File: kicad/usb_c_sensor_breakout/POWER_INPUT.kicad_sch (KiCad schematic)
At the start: 5 parts, among them J1 USB_C_Receptacle_PowerOnly_6P

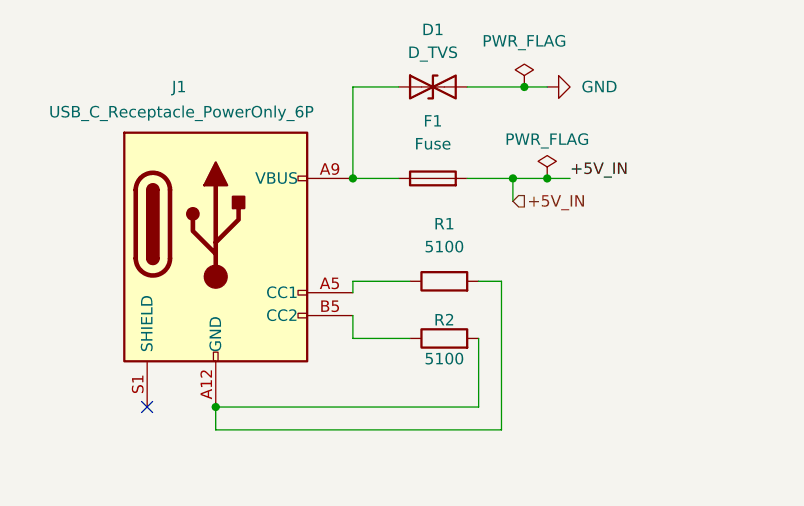
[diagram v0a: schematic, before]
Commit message: Commit3: Regulators + Top-level + I2C sensor upgrade
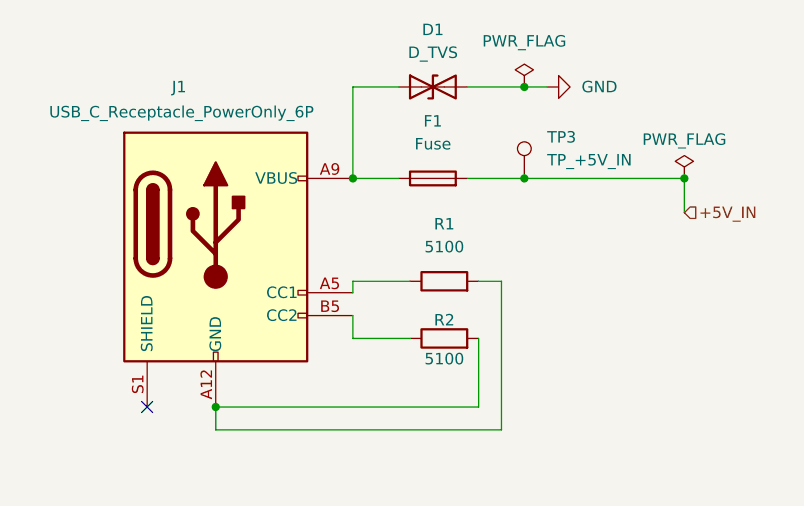
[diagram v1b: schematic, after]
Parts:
- added TP3: TP_+5V_IN, symbol Connector:TestPoint
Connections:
- net +5V_IN: now also TP3.1
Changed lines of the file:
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@@
 	(paper "A4")
-	(junction
-		(at 119.38 83.82)
-		(diameter 0)
-		(color 0 0 0 0)
-	)
 	(junction
 		(at 82.55 109.22)
@@
 	)
 	(junction
-		(at 115.57 83.82)
+		(at 116.84 83.82)
+		(diameter 0)
+		(color 0 0 0 0)
+	)
+	(junction
+		(at 134.62 83.82)
 		(diameter 0)
 		(color 0 0 0 0)
@@
 	(wire
 		(pts
-			(xy 115.57 83.82) (xy 119.38 83.82)
-		)
-		(stroke
-			(width 0)
-			(type default)
-		)
-	)
-	(wire
-		(pts
 			(xy 116.84 73.66) (xy 119.38 73.66)
 		)
@@
 	(wire
 		(pts
+			(xy 116.84 83.82) (xy 134.62 83.82)
+		)
+		(stroke
+			(width 0)
+			(type default)
+		)
+	)
+	(wire
+		(pts
 			(xy 97.79 83.82) (xy 97.79 73.66)
 		)
@@
 	(wire
 		(pts
-			(xy 119.38 83.82) (xy 121.92 83.82)
-		)
-		(stroke
-			(width 0)
-			(type default)
-		)
-	)
-	(wire
-		(pts
 			(xy 97.79 73.66) (xy 102.87 73.66)
 		)
@@
 	(wire
 		(pts
-			(xy 115.57 86.36) (xy 115.57 83.82)
+			(xy 134.62 83.82) (xy 134.62 87.63)
 		)
 		(stroke
@@
 	(wire
 		(pts
-			(xy 110.49 83.82) (xy 115.57 83.82)
-		)
-		(stroke
-			(width 0)
-			(type default)
-		)
-	)
-	(label "+5V_IN"
-		(at 121.92 83.82 0)
-		(effects
-			(font
-				(size 1.27 1.27)
-			)
-			(justify left bottom)
+			(xy 110.49 83.82) (xy 116.84 83.82)
+		)
+		(stroke
+			(width 0)
+			(type default)
 		)
 	)
 	(hierarchical_label "+5V_IN"
 		(shape input)
-		(at 115.57 86.36 0)
+		(at 134.62 87.63 0)
 		(effects
 			(font
@@
 	(symbol
 		(lib_id "power:PWR_FLAG")
-		(at 119.38 83.82 0)
+		(at 134.62 83.82 0)
 		(unit 1)
 		(exclude_from_sim no)
@@
 		(dnp no)
 		(property "Reference" "#FLG0101"
-			(at 119.38 81.915 0)
+			(at 134.62 81.915 0)
 			(effects
 				(font
@@
 		)
 		(property "Value" "PWR_FLAG"
-			(at 119.38 79.502 0)
+			(at 134.62 79.502 0)
 			(effects
 				(font
@@
 		)
 		(property "Footprint" ""
-			(at 119.38 83.82 0)
+			(at 134.62 83.82 0)
 			(effects
 				(font
@@
 		)
 		(property "Datasheet" "~"
-			(at 119.38 83.82 0)
+			(at 134.62 83.82 0)
 			(effects
 				(font
@@
 		)
 		(property "Description" "Special symbol for telling ERC where power comes from"
-			(at 119.38 83.82 0)
+			(at 134.62 83.82 0)
 			(effects
 				(font
@@
 					(unit 1)
 				)
+			)
+		)
+	)
+	(symbol
+		(lib_id "Connector:TestPoint")
+		(at 116.84 83.82 0)
+		(unit 1)
+		(exclude_from_sim no)
+		(in_bom yes)
+		(on_board yes)
+		(dnp no)
+		(fields_autoplaced yes)
+		(property "Reference" "TP3"
+			(at 119.38 79.2479 0)
+			(effects
+				(font
+					(size 1.27 1.27)
+				)
+				(justify left)
+			)
+		)
+		(property "Value" "TP_+5V_IN"
+			(at 119.38 81.7879 0)
+			(effects
+				(font
+					(size 1.27 1.27)
+				)
+				(justify left)
+			)
+		)
+		(property "Footprint" ""
+			(at 121.92 83.82 0)
+			(effects
+				(font
+					(size 1.27 1.27)
+				)
+				(hide yes)
+			)
+		)
+		(property "Datasheet" "~"
+			(at 121.92 83.82 0)
+			(effects
+				(font
+					(size 1.27 1.27)
+				)
+				(hide yes)
+			)
+		)
+		(property "Description" "test point"
+			(at 116.84 83.82 0)
+			(effects
+				(font
+					(size 1.27 1.27)
+				)
+				(hide yes)
+			)
+		)
+		(pin "1"
+		)
+		(instances
+			(project ""
+				(path "/a2072585-dfc7-469c-b616-14a83342abb9/2cb23028-9002-4014-b3cb-b730b7692fef"
+					(reference "TP3")
+					(unit 1)
+				)

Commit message: Commit 4: Updated annotation + footprints
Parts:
- D1: footprint (none) -> Diode_SMD:D_SOD-123
- F1: footprint (none) -> Fuse:Fuse_1812_4532Metric
- J1: footprint (none) -> Connector_USB:USB_C_Receptacle_HRO_TYPE-C-31-M-12
- R1, R2: footprint (none) -> Resistor_SMD:R_0603_1608Metric
- TP3: footprint (none) -> TestPoint:TestPoint_Pad_D1.5mm
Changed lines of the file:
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@@
 			)
 		)
-		(property "Footprint" ""
+		(property "Footprint" "Resistor_SMD:R_0603_1608Metric"
 			(at 107.95 97.028 90)
 			(effects
@@
 			)
 		)
-		(property "Footprint" ""
+		(property "Footprint" "Fuse:Fuse_1812_4532Metric"
 			(at 106.68 85.598 90)
 			(effects
@@
 			)
 		)
-		(property "Footprint" ""
+		(property "Footprint" "Resistor_SMD:R_0603_1608Metric"
 			(at 107.95 103.378 90)
 			(effects
@@
 			)
 		)
-		(property "Footprint" ""
+		(property "Footprint" "Connector_USB:USB_C_Receptacle_HRO_TYPE-C-31-M-12"
 			(at 86.36 88.9 0)
 			(effects
@@
 			)
 		)
-		(property "Footprint" ""
+		(property "Footprint" "Diode_SMD:D_SOD-123"
 			(at 106.68 73.66 0)
 			(effects
@@
 			)
 		)
-		(property "Footprint" ""
+		(property "Footprint" "TestPoint:TestPoint_Pad_D1.5mm"
 			(at 121.92 83.82 0)
 			(effects

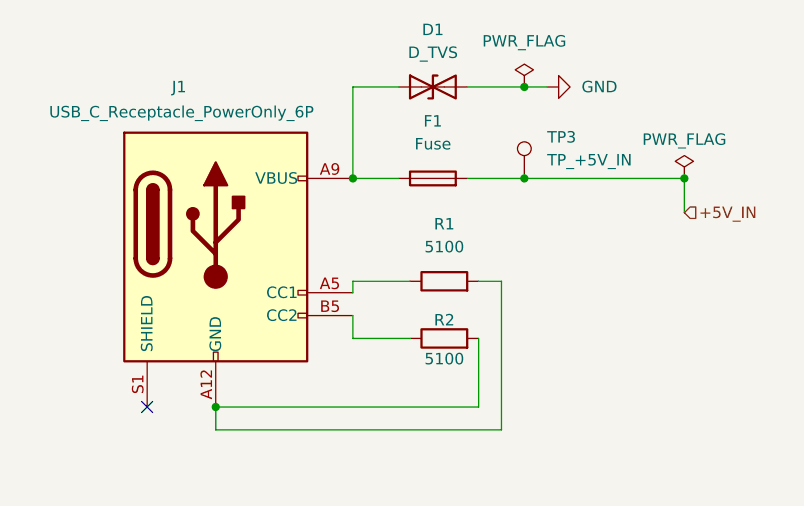
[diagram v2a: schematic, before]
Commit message: Commit 5: MCU + Final Schematic Touches + Labelling + USBc fix
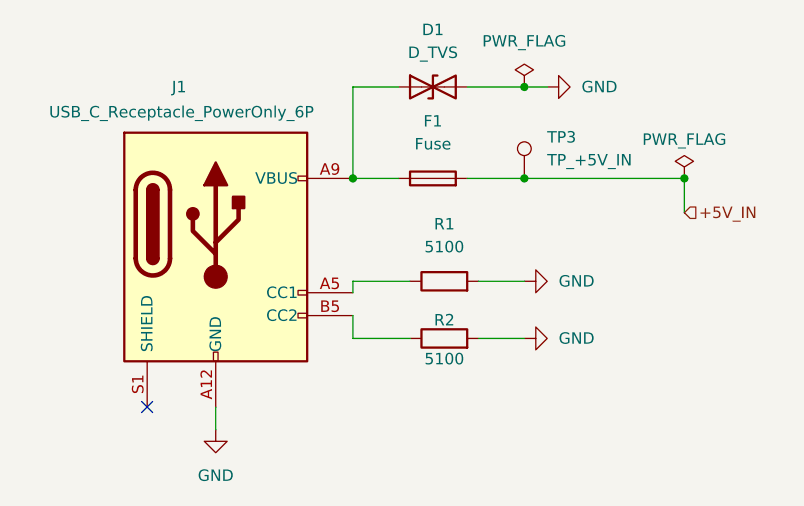
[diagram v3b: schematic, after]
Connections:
- net GND: now also J1.A12 (GND), J1.B12 (GND), R1.2, R2.2
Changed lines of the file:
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@@
 	(paper "A4")
-	(junction
-		(at 82.55 109.22)
-		(diameter 0)
-		(color 0 0 0 0)
-	)
 	(junction
 		(at 116.84 73.66)
@@
 	(wire
 		(pts
-			(xy 114.3 95.25) (xy 114.3 111.76)
-		)
-		(stroke
-			(width 0)
-			(type default)
-		)
-	)
-	(wire
-		(pts
 			(xy 116.84 83.82) (xy 134.62 83.82)
 		)
@@
 	(wire
 		(pts
+			(xy 111.76 101.6) (xy 116.84 101.6)
+		)
+		(stroke
+			(width 0)
+			(type default)
+		)
+	)
+	(wire
+		(pts
 			(xy 97.79 73.66) (xy 102.87 73.66)
 		)
@@
 	(wire
 		(pts
-			(xy 82.55 109.22) (xy 111.76 109.22)
-		)
-		(stroke
-			(width 0)
-			(type default)
-		)
-	)
-	(wire
-		(pts
 			(xy 97.79 95.25) (xy 104.14 95.25)
 		)
@@
 	(wire
 		(pts
-			(xy 114.3 111.76) (xy 82.55 111.76)
-		)
-		(stroke
-			(width 0)
-			(type default)
-		)
-	)
-	(wire
-		(pts
 			(xy 134.62 83.82) (xy 134.62 87.63)
 		)
@@
 	(wire
 		(pts
-			(xy 111.76 109.22) (xy 111.76 101.6)
-		)
-		(stroke
-			(width 0)
-			(type default)
-		)
-	)
-	(wire
-		(pts
-			(xy 111.76 95.25) (xy 114.3 95.25)
-		)
-		(stroke
-			(width 0)
-			(type default)
-		)
-	)
-	(wire
-		(pts
 			(xy 110.49 83.82) (xy 116.84 83.82)
+		)
+		(stroke
+			(width 0)
+			(type default)
+		)
+	)
+	(wire
+		(pts
+			(xy 111.76 95.25) (xy 116.84 95.25)
 		)
 		(stroke
@@
 	)
 	(symbol
+		(lib_id "power:GND")
+		(at 116.84 101.6 90)
+		(unit 1)
+		(exclude_from_sim no)
+		(in_bom yes)
+		(on_board yes)
+		(dnp no)
+		(fields_autoplaced yes)
+		(property "Reference" "#PWR014"
+			(at 123.19 101.6 0)
+			(effects
+				(font
+					(size 1.27 1.27)
+				)
+				(hide yes)
+			)
+		)
+		(property "Value" "GND"
+			(at 120.65 101.5999 90)
+			(effects
+				(font
+					(size 1.27 1.27)
+				)
+				(justify right)
+			)
+		)
+		(property "Footprint" ""
+			(at 116.84 101.6 0)
+			(effects
+				(font
+					(size 1.27 1.27)
+				)
+				(hide yes)
+			)
+		)
+		(property "Datasheet" ""
+			(at 116.84 101.6 0)
+			(effects
+				(font
+					(size 1.27 1.27)
+				)
+				(hide yes)
+			)
+		)
+		(property "Description" "Power symbol creates a global label with name \"GND\" , ground"
+			(at 116.84 101.6 0)
+			(effects
+				(font
+					(size 1.27 1.27)
+				)
+				(hide yes)
+			)
+		)
+		(pin "1"
+		)
+		(instances
+			(project ""
+				(path "/a2072585-dfc7-469c-b616-14a83342abb9/2cb23028-9002-4014-b3cb-b730b7692fef"
+					(reference "#PWR014")
+					(unit 1)
+				)
+			)
+		)
+	)
+	(symbol
 		(lib_id "power:PWR_FLAG")
 		(at 134.62 83.82 0)
@@
 	)
 	(symbol
+		(lib_id "power:GND")
+		(at 82.55 111.76 0)
+		(unit 1)
+		(exclude_from_sim no)
+		(in_bom yes)
+		(on_board yes)
+		(dnp no)
+		(fields_autoplaced yes)
+		(property "Reference" "#PWR013"
+			(at 82.55 118.11 0)
+			(effects
+				(font
+					(size 1.27 1.27)
+				)
+				(hide yes)
+			)
+		)
+		(property "Value" "GND"
+			(at 82.55 116.84 0)
+			(effects
+				(font
+					(size 1.27 1.27)
+				)
+			)
+		)
+		(property "Footprint" ""
+			(at 82.55 111.76 0)
+			(effects
+				(font
+					(size 1.27 1.27)
+				)
+				(hide yes)
+			)
+		)
+		(property "Datasheet" ""
+			(at 82.55 111.76 0)
+			(effects
+				(font
+					(size 1.27 1.27)
+				)
+				(hide yes)
+			)
+		)
+		(property "Description" "Power symbol creates a global label with name \"GND\" , ground"
+			(at 82.55 111.76 0)
+			(effects
+				(font
+					(size 1.27 1.27)
+				)
+				(hide yes)
+			)
+		)
+		(pin "1"
+		)
+		(instances
+			(project ""
+				(path "/a2072585-dfc7-469c-b616-14a83342abb9/2cb23028-9002-4014-b3cb-b730b7692fef"
+					(reference "#PWR013")
+					(unit 1)
+				)
+			)
+		)
+	)
+	(symbol
 		(lib_id "Connector:USB_C_Receptacle_PowerOnly_6P")
 		(at 82.55 91.44 0)
@@
 					(unit 1)
 				)
+			)
+		)
+	)
+	(symbol
+		(lib_id "power:GND")
+		(at 116.84 95.25 90)
+		(unit 1)
+		(exclude_from_sim no)
+		(in_bom yes)
+		(on_board yes)
+		(dnp no)
+		(fields_autoplaced yes)
+		(property "Reference" "#PWR015"
+			(at 123.19 95.25 0)
+			(effects
+				(font
+					(size 1.27 1.27)
+				)
+				(hide yes)
+			)
+		)
+		(property "Value" "GND"
+			(at 120.65 95.2499 90)
+			(effects
+				(font
+					(size 1.27 1.27)
+				)
+				(justify right)
+			)
+		)
+		(property "Footprint" ""
+			(at 116.84 95.25 0)
+			(effects
+				(font
+					(size 1.27 1.27)
+				)
+				(hide yes)
+			)
+		)
+		(property "Datasheet" ""
+			(at 116.84 95.25 0)
+			(effects
+				(font
+					(size 1.27 1.27)
+				)
+				(hide yes)
+			)
+		)
+		(property "Description" "Power symbol creates a global label with name \"GND\" , ground"
+			(at 116.84 95.25 0)
+			(effects
+				(font
+					(size 1.27 1.27)
+				)
+				(hide yes)
+			)
+		)
+		(pin "1"
+		)
+		(instances
+			(project ""
+				(path "/a2072585-dfc7-469c-b616-14a83342abb9/2cb23028-9002-4014-b3cb-b730b7692fef"
+					(reference "#PWR015")
+					(unit 1)
+				)

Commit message: Commit 6: Finished PCB + Updated Schematic
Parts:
- J1: footprint Connector_USB:USB_C_Receptacle_HRO_TYPE-C-31-M-12 -> Connector_USB:USB_C_Receptacle_HRO_TYPE-C-31-M-17
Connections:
- net +5V_IN: now also D1.1 (A1), F1.1, J1.A9 (VBUS), J1.B9 (VBUS)
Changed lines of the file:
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@@
+	)
+	(junction
+		(at 97.79 83.82)
+		(diameter 0)
+		(color 0 0 0 0)
 	)
 	(junction
@@
 		(color 0 0 0 0)
 	)
-	(junction
-		(at 97.79 83.82)
-		(diameter 0)
-		(color 0 0 0 0)
-	)
 	(no_connect
 		(at 74.93 109.22)
@@
 	(wire
 		(pts
+			(xy 135.89 83.82) (xy 134.62 83.82)
+		)
+		(stroke
+			(width 0)
+			(type default)
+		)
+	)
+	(wire
+		(pts
 			(xy 116.84 73.66) (xy 119.38 73.66)
 		)
@@
 	(wire
 		(pts
-			(xy 134.62 83.82) (xy 134.62 87.63)
-		)
-		(stroke
-			(width 0)
-			(type default)
-		)
-	)
-	(wire
-		(pts
 			(xy 110.49 83.82) (xy 116.84 83.82)
 		)
@@
 		)
 	)
+	(label "+5V_IN"
+		(at 97.79 83.82 270)
+		(effects
+			(font
+				(size 1.27 1.27)
+			)
+			(justify right bottom)
+		)
+	)
 	(hierarchical_label "+5V_IN"
-		(shape input)
-		(at 134.62 87.63 0)
+		(shape output)
+		(at 135.89 83.82 0)
 		(effects
 			(font
@@
 			)
 		)
-		(property "Footprint" "Connector_USB:USB_C_Receptacle_HRO_TYPE-C-31-M-12"
+		(property "Footprint" "Connector_USB:USB_C_Receptacle_HRO_TYPE-C-31-M-17"
 			(at 86.36 88.9 0)
 			(effects
